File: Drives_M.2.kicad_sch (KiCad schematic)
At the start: 88 parts, among them IC2 LM61480Q3RPHRQ1, J10 Bus_M.2_Socket_M, J11 Bus_M.2_Socket_M, J12 Bus_M.2_Socket_M, J13 Bus_M.2_Socket_M, M1 M.2 Solder Nut, M10 M.2 Screw, M11 M.2 Solder Nut, M12 M.2 Solder Nut, M13 M.2 Solder Nut, M14 M.2 Solder Nut, M15 M.2 Screw, M16 M.2 Solder Nut, M17 M.2 Solder Nut, M18 M.2 Solder Nut, M19 M.2 Solder Nut, M2 M.2 Solder Nut, M20 M.2 Screw, M3 M.2 Solder Nut, M4 M.2 Solder Nut, M5 M.2 Screw, M6 M.2 Solder Nut, M7 M.2 Solder Nut, M8 M.2 Solder Nut, M9 M.2 Solder Nut, U10 ASEK-32.768KHZ-L-R-T, U9 ASM1184

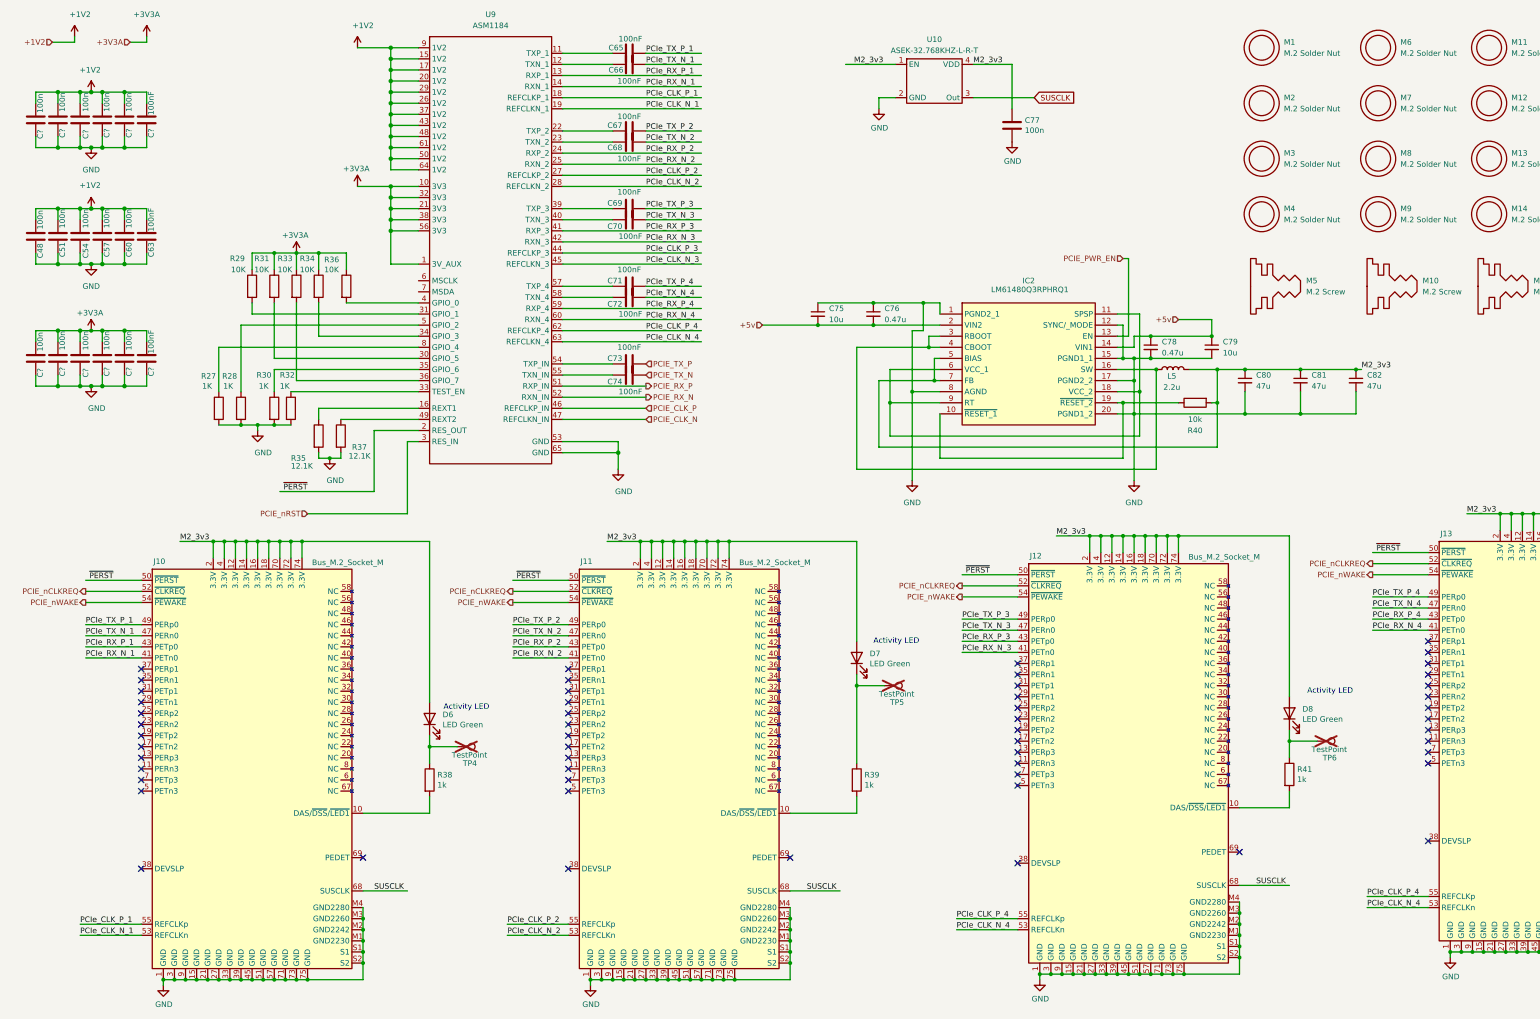
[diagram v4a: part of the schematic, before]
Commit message: Swiitched to JSM561
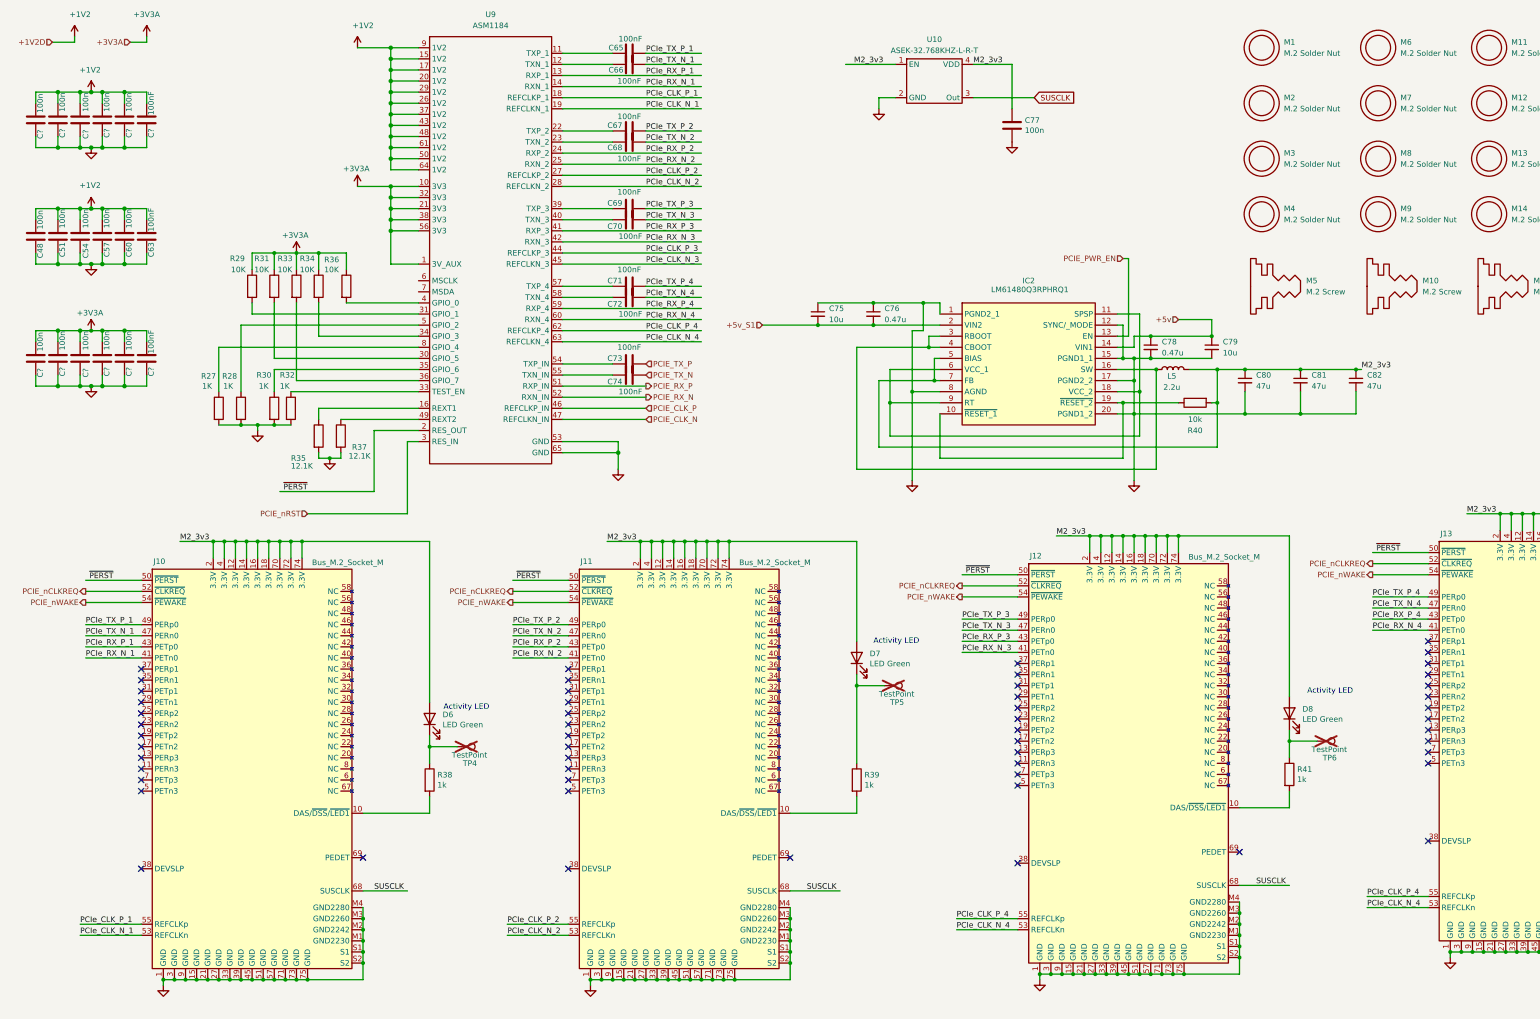
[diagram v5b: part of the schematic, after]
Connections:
- net +5v: no longer C75.2, C76.2, IC2.2 (VIN2)
- removed net GND: C48.2, C51.2, C54.2, C57.2, C60.2, C63.2, C75.1, C76.1, C77.2, C78.2, C79.2, C80.2, C81.2, C82.2, C?.2, C?.2, C?.2, C?.2, C?.2, C?.2, C?.2, C?.2, C?.2, C?.2, C?.2, C?.2, IC2.1 (PGND2_1), IC2.12 (SYNC/_MODE), IC2.15 (PGND1_1), IC2.17 (PGND2_2), IC2.20 (PGND1_2), IC2.8 (AGND), J10.1 (GND), J10.15 (GND), J10.21 (GND), J10.27 (GND), J10.3 (GND), J10.33 (GND), J10.39 (GND), J10.45 (GND), J10.51 (GND), J10.57 (GND), J10.71 (GND), J10.73 (GND), J10.75 (GND), J10.9 (GND), J10.M1 (GND2230), J10.M2 (GND2242), J10.M3 (GND2260), J10.M4 (GND2280), J10.S1, J10.S2, J11.1 (GND), J11.15 (GND), J11.21 (GND), J11.27 (GND), J11.3 (GND), J11.33 (GND), J11.39 (GND), J11.45 (GND), J11.51 (GND), J11.57 (GND), J11.71 (GND), J11.73 (GND), J11.75 (GND), J11.9 (GND), J11.M1 (GND2230), J11.M2 (GND2242), J11.M3 (GND2260), J11.M4 (GND2280), J11.S1, J11.S2, J12.1 (GND), J12.15 (GND), J12.21 (GND), J12.27 (GND), J12.3 (GND), J12.33 (GND), J12.39 (GND), J12.45 (GND), J12.51 (GND), J12.57 (GND), J12.71 (GND), J12.73 (GND), J12.75 (GND), J12.9 (GND), J12.M1 (GND2230), J12.M2 (GND2242), J12.M3 (GND2260), J12.M4 (GND2280), J12.S1, J12.S2, J13.1 (GND), J13.15 (GND), J13.21 (GND), J13.27 (GND), J13.3 (GND), J13.33 (GND), J13.39 (GND), J13.45 (GND), J13.51 (GND), J13.57 (GND), J13.71 (GND), J13.73 (GND), J13.75 (GND), J13.9 (GND), J13.M1 (GND2230), J13.M2 (GND2242), J13.M3 (GND2260), J13.M4 (GND2280), J13.S1, J13.S2, R27.2, R28.2, R30.2, R32.2, R35.2, R37.2, U10.2 (GND), U9.53 (GND), U9.65 (GND)
- new net: R35.2, R37.2
- new net: C?.2, C?.2, C?.2, C?.2, C?.2, C?.2 (x2)
- new net: J10.1 (GND), J10.15 (GND), J10.21 (GND), J10.27 (GND), J10.3 (GND), J10.33 (GND), J10.39 (GND), J10.45 (GND), J10.51 (GND), J10.57 (GND), J10.71 (GND), J10.73 (GND), J10.75 (GND), J10.9 (GND), J10.M1 (GND2230), J10.M2 (GND2242), J10.M3 (GND2260), J10.M4 (GND2280), J10.S1, J10.S2
- new net: J11.1 (GND), J11.15 (GND), J11.21 (GND), J11.27 (GND), J11.3 (GND), J11.33 (GND), J11.39 (GND), J11.45 (GND), J11.51 (GND), J11.57 (GND), J11.71 (GND), J11.73 (GND), J11.75 (GND), J11.9 (GND), J11.M1 (GND2230), J11.M2 (GND2242), J11.M3 (GND2260), J11.M4 (GND2280), J11.S1, J11.S2
- new net: U9.53 (GND), U9.65 (GND)
- new net: C48.2, C51.2, C54.2, C57.2, C60.2, C63.2
- new net: R27.2, R28.2, R30.2, R32.2
- new net: J13.1 (GND), J13.15 (GND), J13.21 (GND), J13.27 (GND), J13.3 (GND), J13.33 (GND), J13.39 (GND), J13.45 (GND), J13.51 (GND), J13.57 (GND), J13.71 (GND), J13.73 (GND), J13.75 (GND), J13.9 (GND), J13.M1 (GND2230), J13.M2 (GND2242), J13.M3 (GND2260), J13.M4 (GND2280), J13.S1, J13.S2
- new net: C75.1, C76.1, IC2.1 (PGND2_1), IC2.8 (AGND)
- new net: C78.2, C79.2, C80.2, C81.2, C82.2, IC2.12 (SYNC/_MODE), IC2.15 (PGND1_1), IC2.17 (PGND2_2), IC2.20 (PGND1_2)
- new net: J12.1 (GND), J12.15 (GND), J12.21 (GND), J12.27 (GND), J12.3 (GND), J12.33 (GND), J12.39 (GND), J12.45 (GND), J12.51 (GND), J12.57 (GND), J12.71 (GND), J12.73 (GND), J12.75 (GND), J12.9 (GND), J12.M1 (GND2230), J12.M2 (GND2242), J12.M3 (GND2260), J12.M4 (GND2280), J12.S1, J12.S2
- new net +5v_S1: C75.2, C76.2, IC2.2 (VIN2)
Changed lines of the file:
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@@
 		)
 	)
-	(hierarchical_label "+5v"
+	(hierarchical_label "+5v_S1"
 		(shape input)
 		(at 182.88 86.36 180)
@@
 		)
 	)
-	(hierarchical_label "+1V2"
+	(hierarchical_label "+1V2D"
 		(shape input)
 		(at 20.32 21.59 180)
@@
 			)
 		)
-		(property "Value" "GND"
+		(property "Value" "~"
 			(at 29.21 50.8 0)
 			(effects
@@
 			)
 		)
-		(property "Value" "GND"
+		(property "Value" "~"
 			(at 30.48 105.41 0)
 			(effects
@@
 			)
 		)
-		(property "Value" "GND"
+		(property "Value" "~"
 			(at 29.21 77.47 0)
 			(effects
@@
 			)
 		)
-		(property "Value" "GND"
+		(property "Value" "~"
 			(at 68.58 115.57 0)
 			(effects
@@
 			)
 		)
-		(property "Value" "GND"
+		(property "Value" "~"
 			(at 45.847 241.8842 0)
 			(effects
@@
 			)
 		)
-		(property "Value" "GND"
+		(property "Value" "~"
 			(at 143.637 241.8842 0)
 			(effects
@@
 			)
 		)
-		(property "Value" "GND"
+		(property "Value" "~"
 			(at 246.507 240.6142 0)
 			(effects
@@
 			)
 		)
-		(property "Value" "GND"
+		(property "Value" "~"
 			(at 340.487 235.5342 0)
 			(effects
@@
 			)
 		)
-		(property "Value" "GND"
+		(property "Value" "~"
 			(at 151.13 124.46 0)
 			(effects
@@
 			)
 		)
-		(property "Value" "GND"
+		(property "Value" "~"
 			(at 85.09 121.92 0)
 			(effects
@@
 			)
 		)
-		(property "Value" "GND"
+		(property "Value" "~"
 			(at 240.157 48.8442 0)
 			(effects
@@
 			)
 		)
-		(property "Value" "GND"
+		(property "Value" "~"
 			(at 209.677 41.2242 0)
 			(effects
@@
 			)
 		)
-		(property "Value" "GND"
+		(property "Value" "~"
 			(at 267.97 127 0)
 			(effects
@@
 			)
 		)
-		(property "Value" "GND"
+		(property "Value" "~"
 			(at 217.17 127 0)
 			(effects

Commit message: Removed Ethernet
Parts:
- removed TP5, TP6, TP7: TestPoint, TestPoint:TestPoint_Pad_2.0x2.0mm, symbol Connector:TestPoint
- TP4: now fitted

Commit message: Sheets neatened
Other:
- moved on the sheet: D9, J13, M1, M10, M11, M12, M13, M14, M15, M16, M17, M18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

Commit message: More Fans
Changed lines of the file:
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@@
 	(rectangle
 		(start 12.7 13.97)
-		(end 49.53 102.87)
+		(end 49.53 109.22)
 		(stroke
 			(width 1)
@@
 		)
 	)
+	(text_box "Clock\n"
+		(exclude_from_sim no)
+		(at 209.55 41.91 0)
+		(size 27.94 9.525)
+		(margins 1.9049 1.9049 1.9049 1.9049)
+		(stroke
+			(width -0.0001)
+			(type solid)
+		)
+		(fill
+			(type none)
+		)
+		(effects
+			(font
+				(face "Times New Roman")
+				(size 2 2)
+				(thickness 0.3175)
+				(color 162 22 34 1)
+			)
+			(justify bottom)
+		)
+	)
+	(text_box "M.2 Mounting\n"
+		(exclude_from_sim no)
+		(at 356.87 66.04 0)
+		(size 27.94 9.525)
+		(margins 1.9049 1.9049 1.9049 1.9049)
+		(stroke
+			(width -0.0001)
+			(type solid)
+		)
+		(fill
+			(type none)
+		)
+		(effects
+			(font
+				(face "Times New Roman")
+				(size 2 2)
+				(thickness 0.3175)
+				(color 162 22 34 1)
+			)
+			(justify bottom)
+		)
+	)
+	(text_box "M.2 Drives\n"
+		(exclude_from_sim no)
+		(at 16.51 129.54 0)
+		(size 27.94 9.525)
+		(margins 1.9049 1.9049 1.9049 1.9049)
+		(stroke
+			(width -0.0001)
+			(type solid)
+		)
+		(fill
+			(type none)
+		)
+		(effects
+			(font
+				(face "Times New Roman")
+				(size 2 2)
+				(thickness 0.3175)
+				(color 162 22 34 1)
+			)
+			(justify bottom)
+		)
+	)
+	(text_box "M.2 Power\n"
+		(exclude_from_sim no)
+		(at 269.24 67.31 0)
+		(size 27.94 9.525)
+		(margins 1.9049 1.9049 1.9049 1.9049)
+		(stroke
+			(width -0.0001)
+			(type solid)
+		)
+		(fill
+			(type none)
+		)
+		(effects
+			(font
+				(face "Times New Roman")
+				(size 2 2)
+				(thickness 0.3175)
+				(color 162 22 34 1)
+			)
+			(justify bottom)
+		)
+	)
+	(text_box "ASM1184"
+		(exclude_from_sim no)
+		(at 106.68 119.38 0)
+		(size 27.94 9.525)
+		(margins 1.9049 1.9049 1.9049 1.9049)
+		(stroke
+			(width -0.0001)
+			(type solid)
+		)
+		(fill
+			(type none)
+		)
+		(effects
+			(font
+				(face "Times New Roman")
+				(size 2 2)
+				(thickness 0.3175)
+				(color 162 22 34 1)
+			)
+			(justify bottom)
+		)
+	)
+	(text_box "Filtering"
+		(exclude_from_sim no)
+		(at 15.24 100.33 0)
+		(size 27.94 9.525)
+		(margins 1.9049 1.9049 1.9049 1.9049)
+		(stroke
+			(width -0.0001)
+			(type solid)
+		)
+		(fill
+			(type none)
+		)
+		(effects
+			(font
+				(face "Times New Roman")
+				(size 2 2)
+				(thickness 0.3175)
+				(color 162 22 34 1)
+			)
+			(justify bottom)
+		)
+	)
